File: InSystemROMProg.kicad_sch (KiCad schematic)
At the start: 6 parts, among them J1 Conn_02x14_Counter_Clockwise, J2 Conn_02x20_Counter_Clockwise, J3 Conn_01x05, U1 SST39SF040-70-4C-PHE

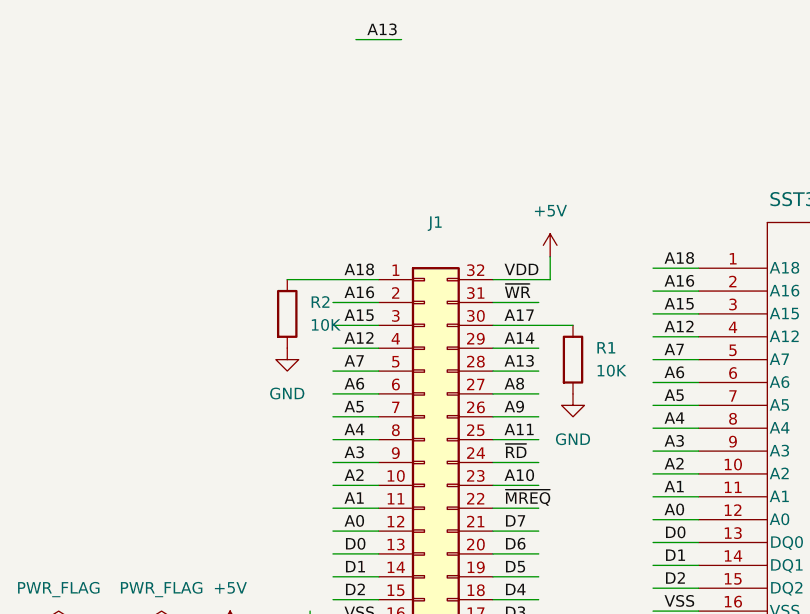
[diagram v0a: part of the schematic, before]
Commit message: Version 1.1 - pinout and pullups fixed, but untested
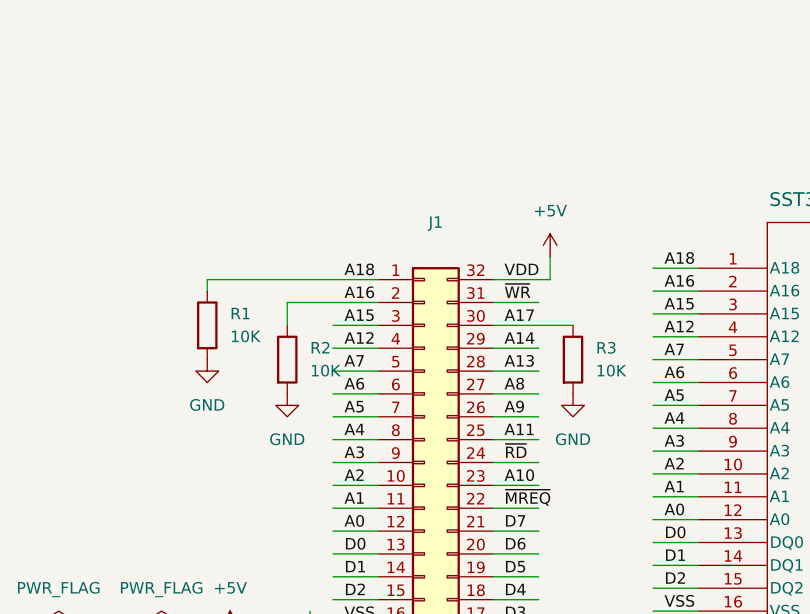
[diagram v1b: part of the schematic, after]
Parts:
- added R2: 10K, Resistor_THT:R_Axial_DIN0207_L6.3mm_D2.5mm_P7.62mm_Horizontal, symbol Device:R
- J2: footprint Connector_PinHeader_2.54mm:PinHeader_2x20_P2.54mm_Vertical -> JgalakLib:PinHeader_2x20_P2.54mm_Vertical
- renumbered R2 to R1, R1 to R3
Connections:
- net A16: now also R2.1
- net GND: now also R2.2
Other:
- moved on the sheet: R1
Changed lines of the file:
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@@
+	(wire
+		(pts
+			(xy 69.85 54.61) (xy 80.01 54.61)
+		)
+		(stroke
+			(width 0)
+			(type default)
+		)
+	)
 	(wire
 		(pts
@@
 	(wire
 		(pts
-			(xy 69.85 52.07) (xy 80.01 52.07)
+			(xy 60.96 52.07) (xy 80.01 52.07)
 		)
 		(stroke
@@
 	(wire
 		(pts
-			(xy 77.47 25.4) (xy 82.55 25.4)
-		)
-		(stroke
-			(width 0)
-			(type default)
-		)
-	)
-	(wire
-		(pts
 			(xy 189.23 86.36) (xy 194.31 86.36)
 		)
@@
 	(wire
 		(pts
-			(xy 74.93 54.61) (xy 80.01 54.61)
-		)
-		(stroke
-			(width 0)
-			(type default)
-		)
-	)
-	(wire
-		(pts
 			(xy 189.23 83.82) (xy 194.31 83.82)
 		)
@@
 	(wire
 		(pts
+			(xy 69.85 54.61) (xy 69.85 57.15)
+		)
+		(stroke
+			(width 0)
+			(type default)
+		)
+	)
+	(wire
+		(pts
 			(xy 156.21 83.82) (xy 161.29 83.82)
 		)
@@
 		(pts
 			(xy 143.51 104.14) (xy 151.13 104.14)
+		)
+		(stroke
+			(width 0)
+			(type default)
+		)
+	)
+	(wire
+		(pts
+			(xy 60.96 52.07) (xy 60.96 53.34)
 		)
 		(stroke
@@
 	(label "A4"
 		(at 111.76 68.58 0)
-		(effects
-			(font
-				(size 1.27 1.27)
-			)
-			(justify left bottom)
-		)
-	)
-	(label "A13"
-		(at 78.74 25.4 0)
 		(effects
 			(font
@@
 			)
 		)
-		(property "Footprint" "Connector_PinHeader_2.54mm:PinHeader_2x20_P2.54mm_Vertical"
+		(property "Footprint" "JgalakLib:PinHeader_2x20_P2.54mm_Vertical"
 			(at 181.61 71.12 0)
 			(effects
@@
 				(path "/e179dc28-e6d0-4d25-b873-7f2990587c66"
 					(reference "J2")
+					(unit 1)
+				)
+			)
+		)
+	)
+	(symbol
+		(lib_id "Device:R")
+		(at 69.85 60.96 0)
+		(unit 1)
+		(exclude_from_sim no)
+		(in_bom yes)
+		(on_board yes)
+		(dnp no)
+		(fields_autoplaced yes)
+		(property "Reference" "R2"
+			(at 72.39 59.6899 0)
+			(effects
+				(font
+					(size 1.27 1.27)
+				)
+				(justify left)
+			)
+		)
+		(property "Value" "10K"
+			(at 72.39 62.2299 0)
+			(effects
+				(font
+					(size 1.27 1.27)
+				)
+				(justify left)
+			)
+		)
+		(property "Footprint" "Resistor_THT:R_Axial_DIN0207_L6.3mm_D2.5mm_P7.62mm_Horizontal"
+			(at 68.072 60.96 90)
+			(effects
+				(font
+					(size 1.27 1.27)
+				)
+				(hide yes)
+			)
+		)
+		(property "Datasheet" "~"
+			(at 69.85 60.96 0)
+			(effects
+				(font
+					(size 1.27 1.27)
+				)
+				(hide yes)
+			)
+		)
+		(property "Description" "Resistor"
+			(at 69.85 60.96 0)
+			(effects
+				(font
+					(size 1.27 1.27)
+				)
+				(hide yes)
+			)
+		)
+		(pin "1"
+		)
+		(pin "2"
+		)
+		(instances
+			(project "InSystemROMProg"
+				(path "/e179dc28-e6d0-4d25-b873-7f2990587c66"
+					(reference "R2")
 					(unit 1)
 				)
@@
 		(dnp no)
 		(fields_autoplaced yes)
-		(property "Reference" "R1"
+		(property "Reference" "R3"
 			(at 104.14 59.6899 0)
 			(effects
@@
 			(project ""
 				(path "/e179dc28-e6d0-4d25-b873-7f2990587c66"
-					(reference "R1")
+					(reference "R3")
 					(unit 1)
 				)
@@
 	)
 	(symbol
+		(lib_id "power:GND")
+		(at 69.85 64.77 0)
+		(unit 1)
+		(exclude_from_sim no)
+		(in_bom yes)
+		(on_board yes)
+		(dnp no)
+		(fields_autoplaced yes)
+		(property "Reference" "#PWR07"
+			(at 69.85 71.12 0)
+			(effects
+				(font
+					(size 1.27 1.27)
+				)
+				(hide yes)
+			)
+		)
+		(property "Value" "GND"
+			(at 69.85 69.85 0)
+			(effects
+				(font
+					(size 1.27 1.27)
+				)
+			)
+		)
+		(property "Footprint" ""
+			(at 69.85 64.77 0)
+			(effects
+				(font
+					(size 1.27 1.27)
+				)
+				(hide yes)
+			)
+		)
+		(property "Datasheet" ""
+			(at 69.85 64.77 0)
+			(effects
+				(font
+					(size 1.27 1.27)
+				)
+				(hide yes)
+			)
+		)
+		(property "Description" "Power symbol creates a global label with name \"GND\" , ground"
+			(at 69.85 64.77 0)
+			(effects
+				(font
+					(size 1.27 1.27)
+				)
+				(hide yes)
+			)
+		)
+		(pin "1"
+		)
+		(instances
+			(project "InSystemROMProg"
+				(path "/e179dc28-e6d0-4d25-b873-7f2990587c66"
+					(reference "#PWR07")
+					(unit 1)
+				)
+			)
+		)
+	)
+	(symbol
 		(lib_id "power:+5V")
 		(at 63.5 91.44 0)
@@
 	(symbol
 		(lib_id "Device:R")
-		(at 69.85 55.88 0)
+		(at 60.96 57.15 0)
 		(unit 1)
 		(exclude_from_sim no)
@@
 		(dnp no)
 		(fields_autoplaced yes)
-		(property "Reference" "R2"
-			(at 72.39 54.6099 0)
+		(property "Reference" "R1"
+			(at 63.5 55.8799 0)
 			(effects
 				(font
@@
 		)
 		(property "Value" "10K"
-			(at 72.39 57.1499 0)
+			(at 63.5 58.4199 0)
 			(effects
 				(font
@@
 		)
 		(property "Footprint" "Resistor_THT:R_Axial_DIN0207_L6.3mm_D2.5mm_P7.62mm_Horizontal"
-			(at 68.072 55.88 90)
+			(at 59.182 57.15 90)
 			(effects
 				(font
@@
 		)
 		(property "Datasheet" "~"
-			(at 69.85 55.88 0)
+			(at 60.96 57.15 0)
 			(effects
 				(font
@@
 		)
 		(property "Description" "Resistor"
-			(at 69.85 55.88 0)
+			(at 60.96 57.15 0)
 			(effects
 				(font
@@
 			(project "InSystemROMProg"
 				(path "/e179dc28-e6d0-4d25-b873-7f2990587c66"
-					(reference "R2")
+					(reference "R1")
 					(unit 1)
 				)
@@
 	(symbol
 		(lib_id "power:GND")
-		(at 69.85 59.69 0)
+		(at 60.96 60.96 0)
 		(unit 1)
 		(exclude_from_sim no)
@@
 		(fields_autoplaced yes)
 		(property "Reference" "#PWR03"
-			(at 69.85 66.04 0)
+			(at 60.96 67.31 0)
 			(effects
 				(font
@@
 		)
 		(property "Value" "GND"
-			(at 69.85 64.77 0)
+			(at 60.96 66.04 0)
 			(effects
 				(font
@@
 		)
 		(property "Footprint" ""
-			(at 69.85 59.69 0)
+			(at 60.96 60.96 0)
 			(effects
 				(font
@@
 		)
 		(property "Datasheet" ""
-			(at 69.85 59.69 0)
+			(at 60.96 60.96 0)
 			(effects
 				(font
@@
 		)
 		(property "Description" "Power symbol creates a global label with name \"GND\" , ground"
-			(at 69.85 59.69 0)
-			(effects
-				(font
+			(at 60.96 60.96 0)
+			(effects
+				(font
